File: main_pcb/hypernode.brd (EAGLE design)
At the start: 92.5 x 100 mm, 31 parts, among them IC1 74HCT245D, U1 MAX488, X2 JST-XH-CONNECTOR-02-PIN, X4 JST-XH-CONNECTOR-02-PIN, X7 JST-XH-03-PIN-LONG-PAD, X8 JST-XH-03-PIN-LONG-PAD

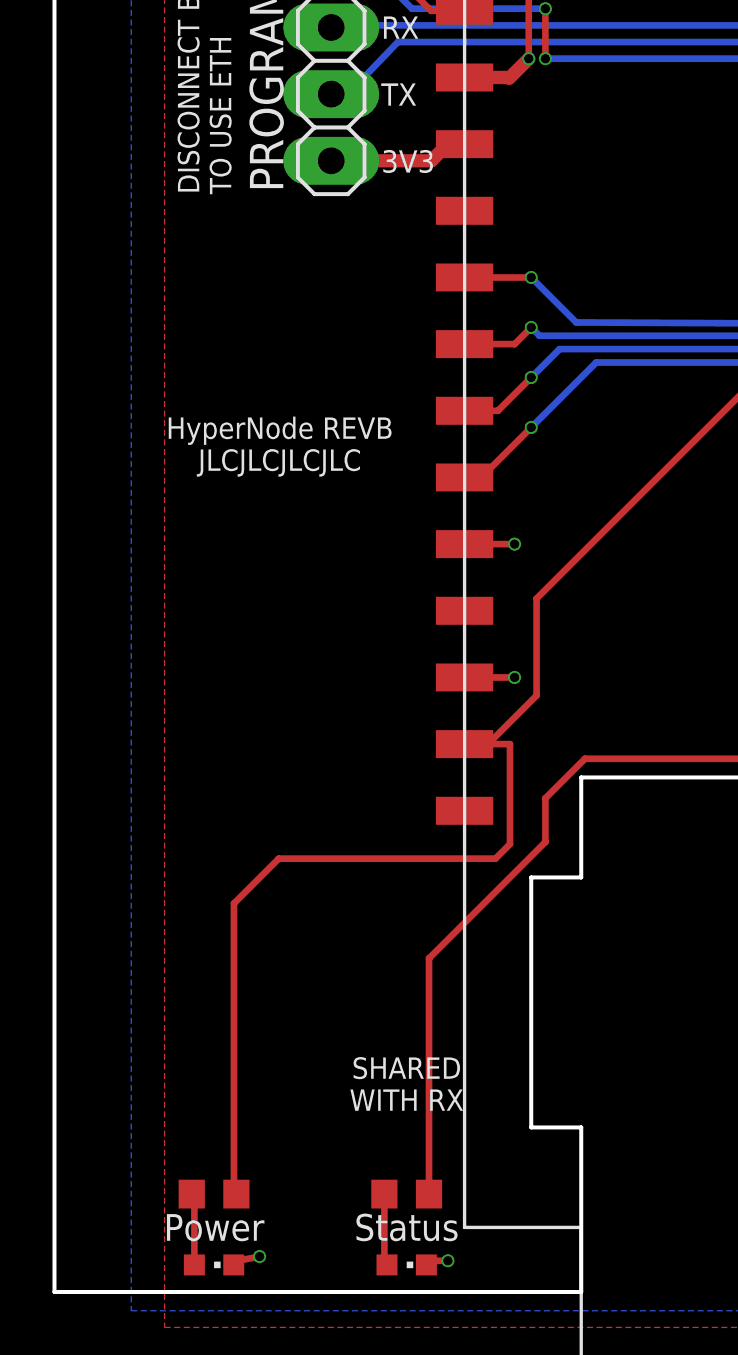
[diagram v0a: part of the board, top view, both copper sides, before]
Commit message: feed power led from 3v3
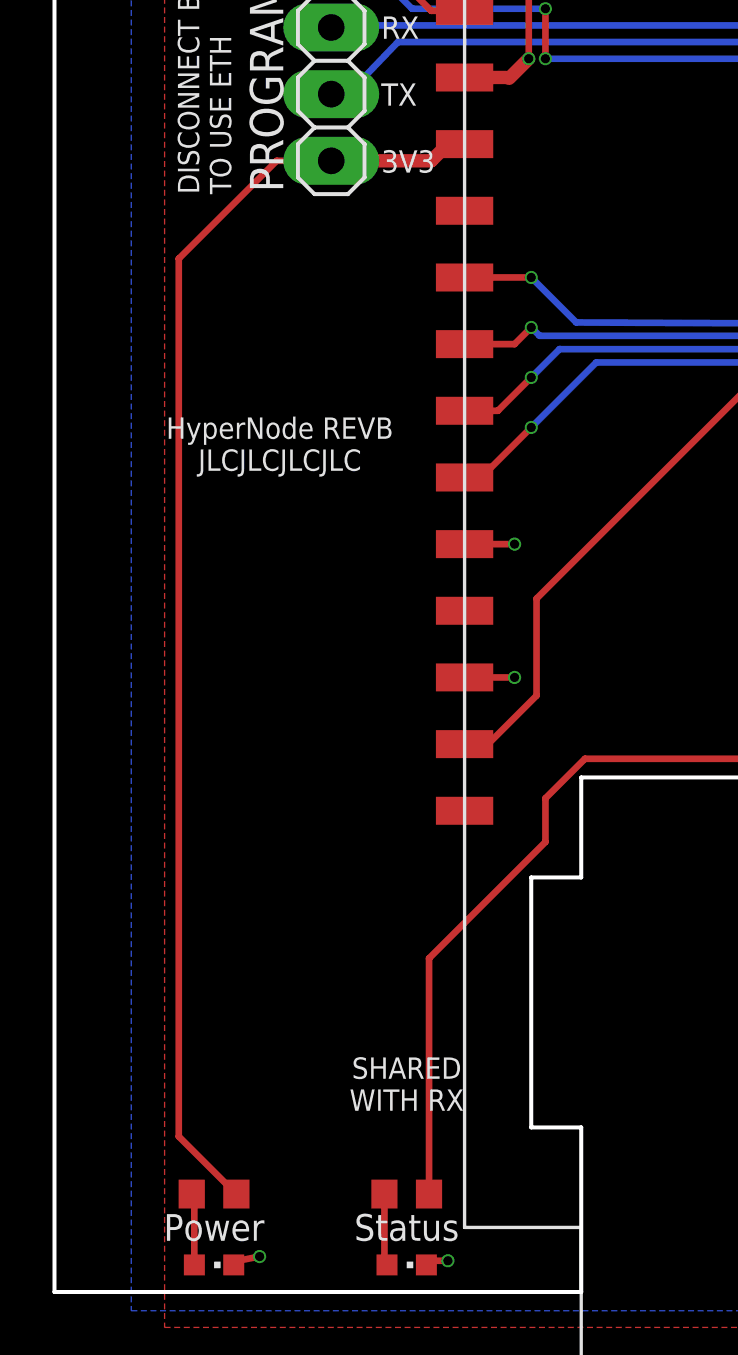
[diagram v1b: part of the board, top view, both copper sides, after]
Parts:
- R51: value 220R -> 180R
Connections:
- net +3V3: now also R51.2
- net +5V: no longer R51.2
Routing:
- net +3V3: track 5.34 -> 49.2 mm
- net +5V: track 162.1 -> 134.0 mm
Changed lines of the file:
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@@
 <attribute name="VALUE" x="57.825" y="66.595" size="0.6096" layer="27" font="vector" align="center"/>
 </element>
-<element name="R51" library="Multischriever" package="ADAFRUIT_R0603" value="220R" x="8.33" y="3.73" smashed="yes">
+<element name="R51" library="Multischriever" package="ADAFRUIT_R0603" value="180R" x="8.33" y="3.73" smashed="yes">
 <attribute name="VALUE" x="8.215" y="5.02" size="0.8128" layer="27" font="vector" align="center"/>
 </element>
@@
 <contactref element="IC1" pad="1"/>
 <contactref element="IC1" pad="20"/>
-<contactref element="R51" pad="2"/>
 <contactref element="X4" pad="1"/>
 <contactref element="U$17" pad="P_5V"/>
@@
 <wire x1="81.16" y1="34.425" x2="82.01" y2="33.575" width="0.254" layer="1"/>
 <wire x1="82.01" y1="33.575" x2="82.01" y2="30.3238" width="0.254" layer="1"/>
-<wire x1="19.605" y1="17.065" x2="19.605" y2="20.875" width="0.254" layer="1"/>
-<wire x1="19.605" y1="17.065" x2="19.05" y2="16.51" width="0.254" layer="1"/>
-<wire x1="19.05" y1="16.51" x2="10.795" y2="16.51" width="0.254" layer="1"/>
-<wire x1="10.795" y1="16.51" x2="9.08806875" y2="14.80306875" width="0.254" layer="1"/>
 <wire x1="67.35" y1="32.8892" x2="67.35" y2="22.8308" width="0.254" layer="1"/>
-<wire x1="19.605" y1="20.875" x2="17.875" y2="20.875" width="0.254" layer="1"/>
-<wire x1="9.08806875" y1="14.80306875" x2="9.08806875" y2="3.82193125" width="0.254" layer="1"/>
-<wire x1="9.08806875" y1="3.82193125" x2="9.18" y2="3.73" width="0.254" layer="1"/>
 <wire x1="67.27964375" y1="38.1" x2="67.27964375" y2="32.95955625" width="0.254" layer="1"/>
 <wire x1="67.27964375" y1="32.95955625" x2="67.35" y2="32.8892" width="0.254" layer="1"/>
@@
 <wire x1="17.24" y1="43.735" x2="16.605" y2="43.1" width="0.508" layer="1"/>
 <wire x1="17.24" y1="43.735" x2="17.875" y2="43.735" width="0.254" layer="1"/>
+<contactref element="R51" pad="2"/>
+<wire x1="12.795" y1="43.1" x2="10.715" y2="43.1" width="0.254" layer="1"/>
+<wire x1="6.985" y1="5.925" x2="9.18" y2="3.73" width="0.254" layer="1"/>
+<wire x1="10.715" y1="43.1" x2="6.985" y2="39.37" width="0.254" layer="1"/>
+<wire x1="6.985" y1="39.37" x2="6.985" y2="5.925" width="0.254" layer="1"/>
 </signal>
 <signal name="N$9">
